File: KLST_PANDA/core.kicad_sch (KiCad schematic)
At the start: 34 parts, among them SW1 BUTTON_RESET, SW2 BUTTON_BOOT_FLASH, U2 STM32H723ZGTx, Y1 16MHz

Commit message: resolved TODOs
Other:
- note removed: "@TODO(check with AN5419 "2.1.1 External power supplies and components", Table 2. Power supply connection)"
- note removed: "@TODO(polarized cap as in MB1246)"
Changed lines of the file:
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@@
-    (effects (font (size 1.27 1.27)) (justify left bottom))
-  )
-  (text "@TODO(check with AN5419 \"2.1.1 External power supplies and components\", Table 2. Power supply connection)\n"
-    (at 157.48 89.535 0)
     (effects (font (size 1.27 1.27)) (justify left bottom))
   )
@@
     (effects (font (size 1.27 1.27)) (justify left bottom))
   )
-  (text "@TODO(polarized cap as in MB1246)" (at 294.64 71.755 0)
-    (effects (font (size 1.27 1.27)) (justify right bottom))
-  )
   (text "BUTTON_BOOT_FLASH" (at 334.645 93.98 0)

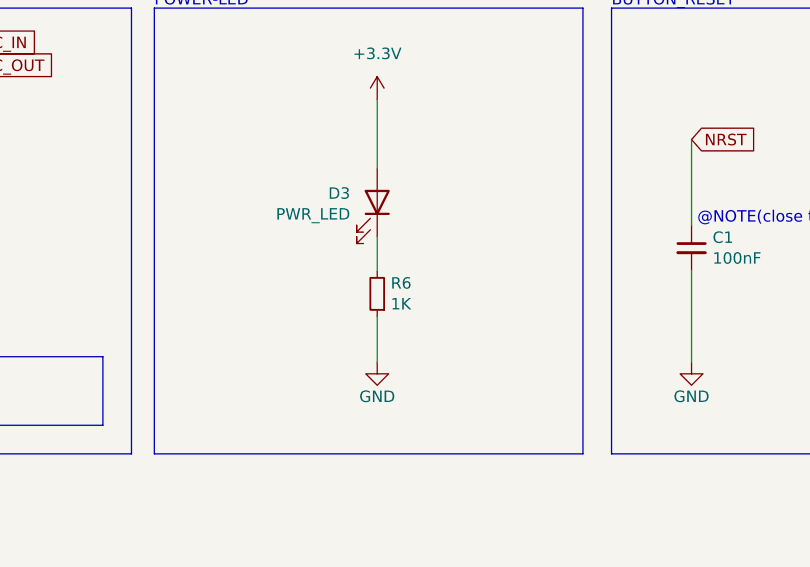
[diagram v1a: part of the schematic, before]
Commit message: started spec'ing components
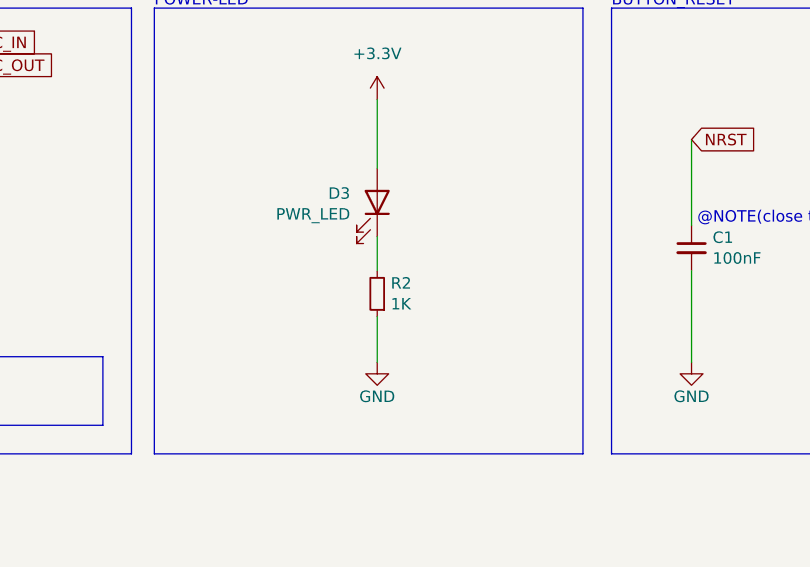
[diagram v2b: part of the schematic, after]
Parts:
- removed R6: 1K, Resistor_SMD:R_0805_2012Metric_Pad1.20x1.40mm_HandSolder, symbol Device:R_Small
- added R2: 1K, Resistor_SMD:R_0805_2012Metric_Pad1.20x1.40mm_HandSolder, symbol Device:R_Small
- C1, C11, C12, C14, C15, C16, C17, C19, C21, C22, C3, C4, C5, C8, C9: JLCPCB (none) -> C1525; JLCPCB Part # C1525 -> (none)
- C10, C6: JLCPCB (none) -> C1547; JLCPCB Part # C1547 -> (none)
- C13, C2, C7: JLCPCB (none) -> C52923; JLCPCB Part # C52923 -> (none)
- C23: footprint (none) -> Capacitor_SMD:C_0402_1005Metric; JLCPCB (none) -> C23733
- C24, C26: footprint Capacitor_SMD:C_0603_1608Metric -> Capacitor_SMD:C_0402_1005Metric; JLCPCB (none) -> C107370; JLCPCB Part # C23630 -> (none)
- D3: JLCPCB (none) -> C34499; JLCPCB Part # C34499 -> (none)
- R3: JLCPCB (none) -> C25077; JLCPCB Part # C25077 -> (none)
- R3, R4: JLCPCB (none) -> C25744; JLCPCB Part # C25744 -> (none)
- R75: footprint (none) -> Resistor_SMD:R_0402_1005Metric; Extended Part (none) -> -; JLCPCB (none) -> C25744
- SW1, SW2: JLCPCB (none) -> C115357; JLCPCB Part # C115357 -> (none)
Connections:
- net GND: now also R2.1
- net at D3.1 (K): now also R2.2

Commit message: assigned footprints
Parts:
- U2: JLCPCB (none) -> C730146; JLCPCB Part # C730146 -> (none)
- Y1: JLCPCB (none) -> C13738; JLCPCB Part # C13738 -> (none)
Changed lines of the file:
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@@
+      (effects (font (size 1.27 1.27)) hide)
+    )
+    (property "Description" "125mW" (at 246.38 125.73 0)
       (effects (font (size 1.27 1.27)) hide)
     )
@@
       (effects (font (size 1.27 1.27)) hide)
     )
-    (property "JLCPCB Part #" "C730146" (at 83.82 123.19 0)
+    (property "JLCPCB Part #" "" (at 83.82 123.19 0)
+      (effects (font (size 1.27 1.27)) hide)
+    )
+    (property "JLCPCB" "C730146" (at 83.82 123.19 0)
       (effects (font (size 1.27 1.27)) hide)
     )
@@
       (effects (font (size 1.27 1.27)) hide)
     )
+    (property "Description" "62.5mW" (at 191.77 105.41 0)
+      (effects (font (size 1.27 1.27)) hide)
+    )
     (pin "1")
     (pin "2")
@@
     )
     (property "JLCPCB" "C25744" (at 311.785 111.76 0)
+      (effects (font (size 1.27 1.27)) hide)
+    )
+    (property "Description" "62.5mW" (at 311.785 111.76 0)
       (effects (font (size 1.27 1.27)) hide)
     )
@@
       (effects (font (size 1.27 1.27)) hide)
     )
+    (property "Description" "62.5mW" (at 337.185 73.66 0)
+      (effects (font (size 1.27 1.27)) hide)
+    )
     (pin "1")
     (pin "2")
@@
       (effects (font (size 1.27 1.27)) hide)
     )
+    (property "Description" "62.5mW" (at 340.995 129.54 0)
+      (effects (font (size 1.27 1.27)) hide)
+    )
     (pin "1")
     (pin "2")
@@
       (effects (font (size 1.27 1.27)) hide)
     )
-    (property "JLCPCB Part #" "C13738" (at 184.15 114.3 0)
-      (effects (font (size 1.27 1.27)) hide)
-    )
+    (property "JLCPCB Part #" "" (at 184.15 114.3 0)
+      (effects (font (size 1.27 1.27)) hide)
+    )
+    (property "Description" "9pF" (at 184.15 114.3 0)
+      (effects (font (size 1.27 1.27)) hide)
+    )
+    (property "JLCPCB" "C13738" (at 184.15 114.3 0)
+      (effects (font (size 1.27 1.27)) hide)
+    )

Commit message: cleaned up footprint assignment
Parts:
- C1, C11, C12, C14, C15, C16, C17, C19, C21, C22, C3, C4, C5, C8, C9: Extended Part - -> (none); MFR.Part # CL05B104KO5NNNC -> (none)
- C10, C6: Extended Part - -> (none); MFR.Part # 0402CG120J500NT -> (none)
- C13, C2, C7: Extended Part - -> (none); MFR.Part # CL05A105KA5NQNC -> (none)
- C24, C26: Extended Part - -> (none); MFR.Part # CL10A225KO8NNNC -> (none)
- D3: footprint LED_SMD:LED_0805_2012Metric_Pad1.15x1.40mm_HandSolder -> LED_SMD:LED_0805_2012Metric; Extended Part - -> (none); MFR.Part # C34499 -> (none)
- R3: Extended Part - -> (none); MFR.Part # 0402WGF100JTCE -> (none)
- R3, R4: Extended Part - -> (none); MFR.Part # 0402WGF1002TCE -> (none)
- R75: Extended Part - -> (none)
- SW1, SW2: Extended Part x -> (none); MFR.Part # SKRKAEE020 -> (none)
- Y1: Extended Part - -> (none); MFR.Part # X322516MLB4SI -> (none)

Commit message: distributed modules
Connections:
- net (PWR_LED): now reaches D3.1 (K), R2.2
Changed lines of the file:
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@@
+    (effects (font (size 1.27 1.27)) (justify left bottom))
+  )
+  (label "(PWR_LED)" (at 246.38 121.285 0) (fields_autoplaced)
     (effects (font (size 1.27 1.27)) (justify left bottom))
   )

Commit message: continued routing
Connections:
- net _USB_DEVICE_HOST_MINUS renamed _USB_DEVICE_HOST_N
- net _USB_DEVICE_HOST_PLUS renamed _USB_DEVICE_HOST_P
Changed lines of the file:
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@@
     )
   )
-  (global_label "_USB_DEVICE_HOST_PLUS" (shape input) (at 119.38 67.31 0) (fields_autoplaced)
+  (global_label "_USB_DEVICE_HOST_P" (shape input) (at 119.38 67.31 0) (fields_autoplaced)
     (effects (font (size 1.27 1.27)) (justify left))
     (property "Intersheetrefs" "${INTERSHEET_REFS}" (at 146.2532 67.31 0)
@@
     )
   )
-  (global_label "_USB_DEVICE_HOST_MINUS" (shape input) (at 119.38 64.77 0) (fields_autoplaced)
+  (global_label "_USB_DEVICE_HOST_N" (shape input) (at 119.38 64.77 0) (fields_autoplaced)
     (effects (font (size 1.27 1.27)) (justify left))
     (property "Intersheetrefs" "${INTERSHEET_REFS}" (at 147.3418 64.77 0)

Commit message: started updating PCB
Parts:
- renumbered C7 to C10, C8 to C11, C9 to C12, C10 to C13, C11 to C14, C12 to C15, C13 to C16, C14 to C17, C15 to C18, C16 to C19, C17 to C20, C19 to C21, C21 to C22, C22 to C23, C1 to C25, C23 to C26, C26 to C27, C13 to C28, C2 to C5, C3 to C6, C4 to C7, C5 to C8, C6 to C9, R75 to R10, R4 to R11, R3 to R7, R2 to R8, R3 to R9
